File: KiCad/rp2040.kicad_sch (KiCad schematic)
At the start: 28 parts, among them U4 AP2112K-3.3, U5 GD25Q16xS, U6 RP2040, Y1 XYDBPCNANF-12MHZ

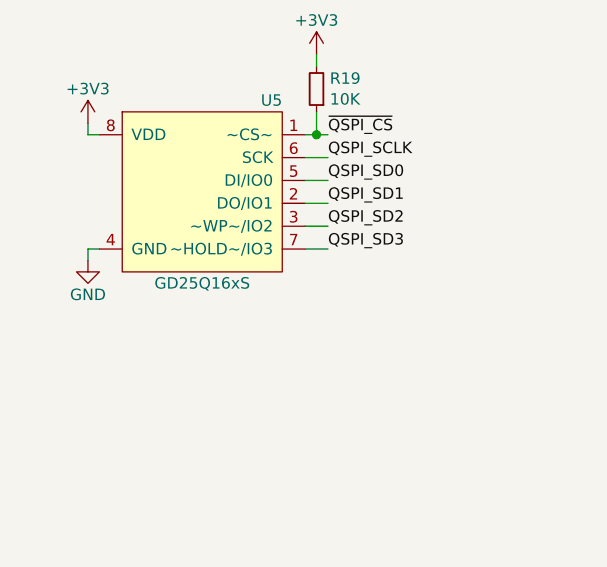
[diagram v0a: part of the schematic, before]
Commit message: Swapping NOR chip for equivalent
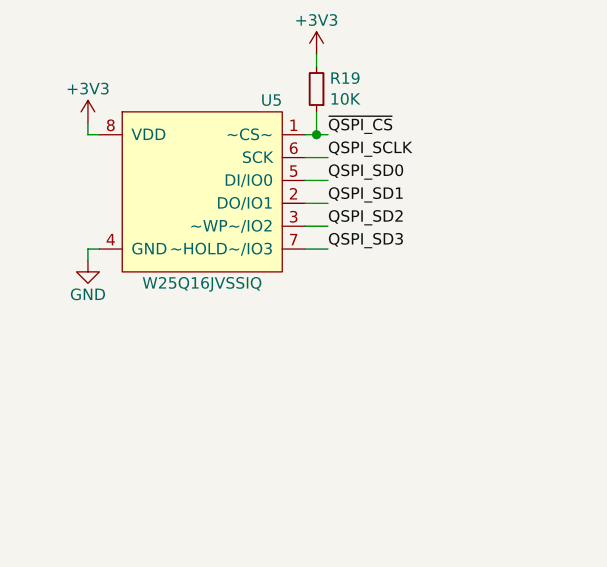
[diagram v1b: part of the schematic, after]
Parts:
- U5: value GD25Q16xS -> W25Q16JVSSIQ; LCSC C79074 -> C131025
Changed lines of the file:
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@@
 			)
 		)
-		(property "Value" "GD25Q16xS"
+		(property "Value" "W25Q16JVSSIQ"
 			(at 41.8592 102.5652 0)
 			(effects
@@
 			)
 		)
-		(property "LCSC" "C79074"
+		(property "LCSC" "C131025"
 			(at 41.8592 92.4052 0)
 			(effects
